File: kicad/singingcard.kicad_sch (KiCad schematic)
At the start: 16 parts, among them J2 Audio_In, SW1 Button, U1 ISD3900FYI, U2 W25Q16JVSSIQ

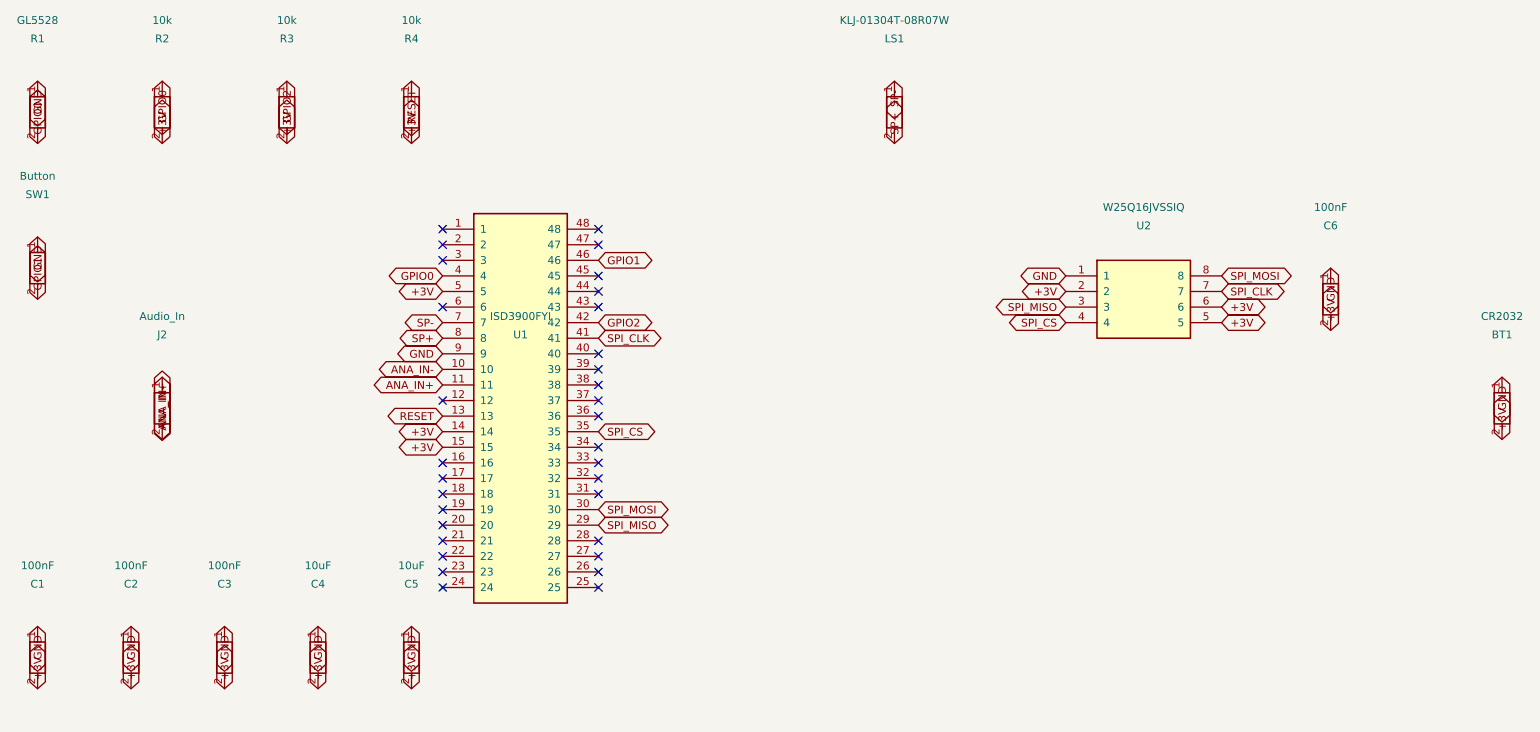
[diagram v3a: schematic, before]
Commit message: Fix global label orientation and U2 3D model offset
Schematic label fixes:
- Fixed label position formula: now uses x + offset*cos(angle) and
  y - offset*sin(angle) to properly offset labels away from components
- Fixed label angle: now uses (angle + 180) % 360 so arrow points
  toward the pin, not away from it
- This resolves labels on left side of chips overlapping with pins
- ERC reduced from 15 to 12 warnings (removed net conflict warnings)

Footprint fixes:
- Fixed U2 (W25Q16JVSSIQ) 3D model offset from (1.65, -2.84, 0) to (0, 0, 0)
- Updated model path to use ${KIPRJMOD} prefix

Skill file updates:
- Updated global label orientation section with correct formulas
- Added "Common mistake" note about Y-axis sign convention
- Added "3D models offset from footprint" troubleshooting section
- Documented easyeda2kicad offset issues and fix

🤖 Generated with [Claude Code](https://claude.com/claude-code)

Co-Authored-By: Claude <noreply@anthropic.com>
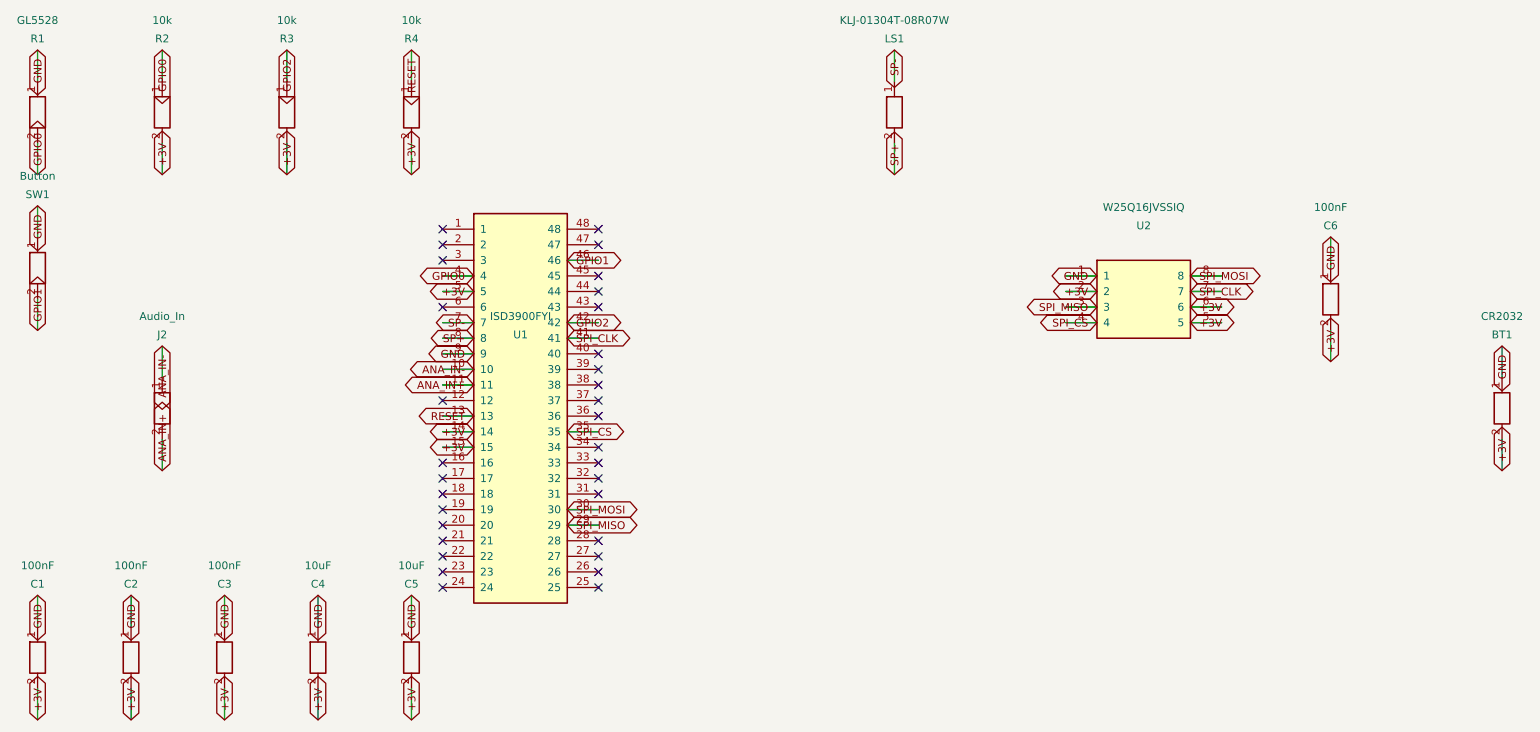
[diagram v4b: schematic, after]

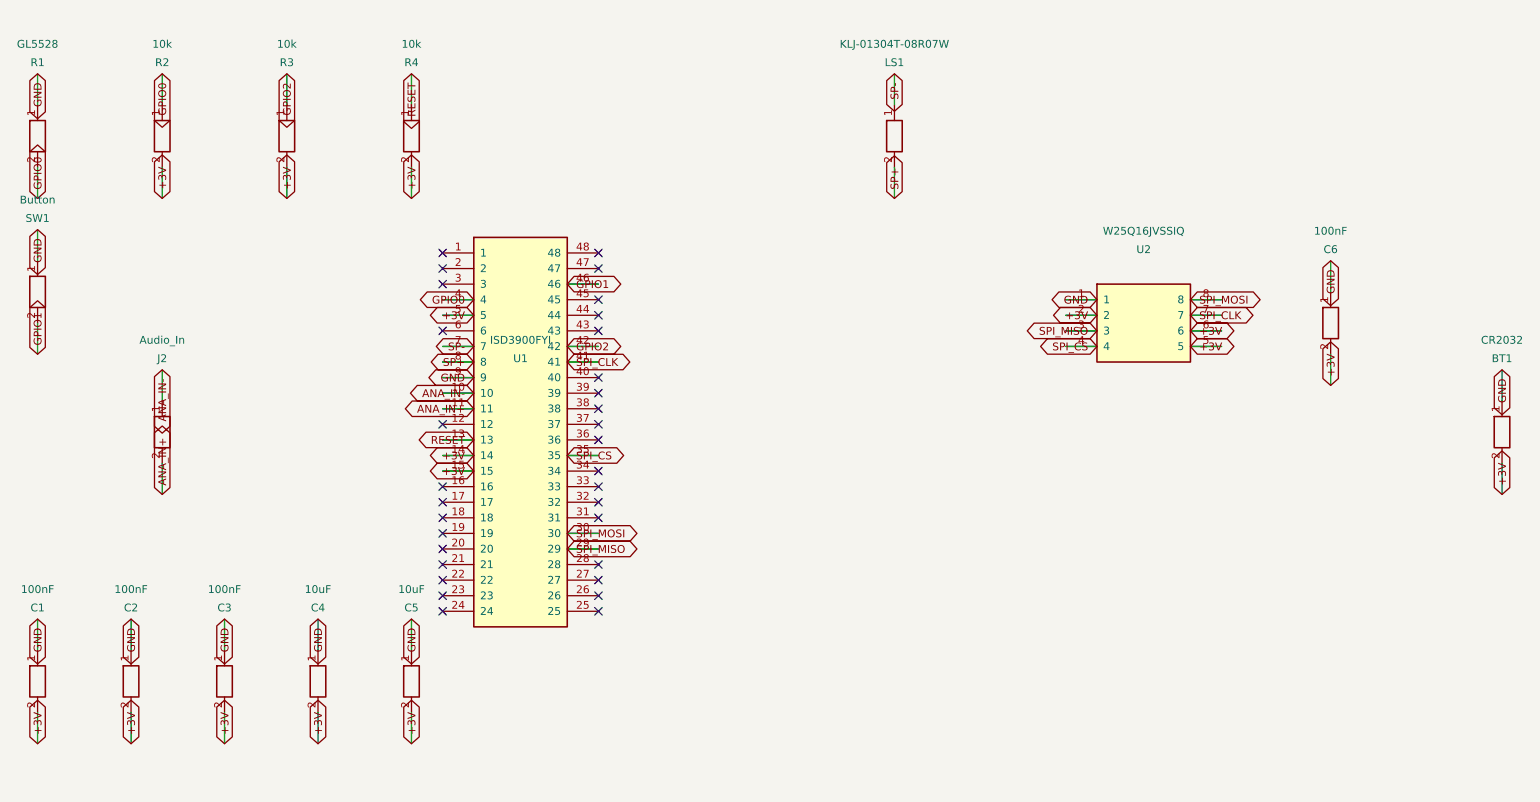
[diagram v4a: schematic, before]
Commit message: Fix global label orientation formula (iteration 2)
Corrected the label placement formula:
- Pin angle points TOWARD component body, not away
- Label offset should be OPPOSITE to pin angle direction
- X formula: x - offset * cos(angle)
- Y formula: y - offset * sin(angle)
- Label angle: same as pin angle (arrow points toward pin)

Labels now correctly placed:
- Left-side IC pins: labels to the LEFT, pointing right
- Right-side IC pins: labels to the RIGHT, pointing left
- Top 2-pin: labels ABOVE, pointing down
- Bottom 2-pin: labels BELOW, pointing up

ERC: 0 errors, 12 warnings (library path warnings only)

🤖 Generated with [Claude Code](https://claude.com/claude-code)

Co-Authored-By: Claude <noreply@anthropic.com>
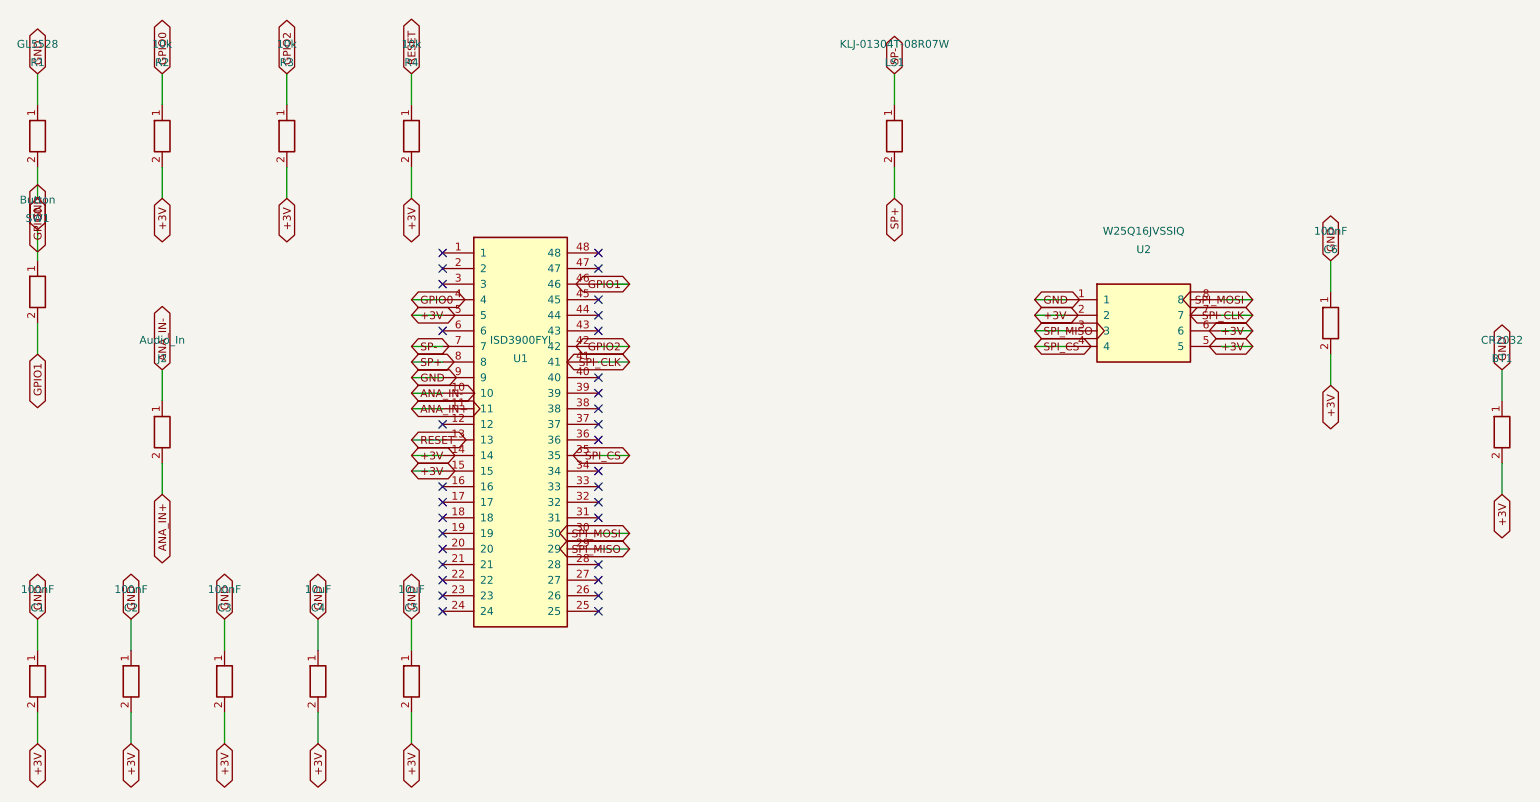
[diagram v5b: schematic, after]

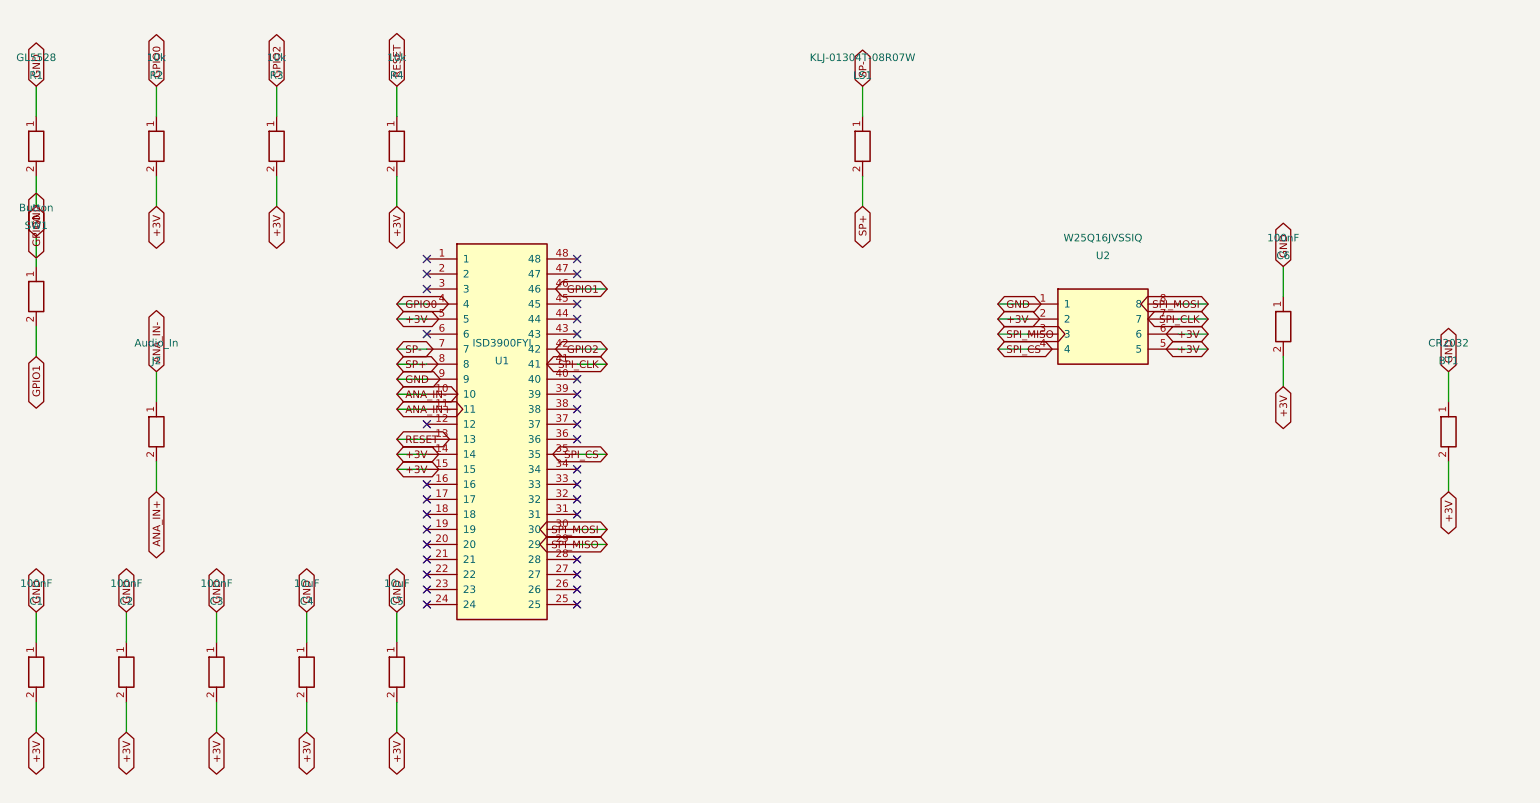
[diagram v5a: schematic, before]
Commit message: Improve schematic readability
Changes:
- Increased label offset from 5.08mm to 7.62mm for better spacing
- Moved reference/value for 2-pin components to the right side
  to avoid overlap with top/bottom pin labels
- Reference designators now clearly visible next to components
- Labels properly separated from component bodies

All 2-pin components (R1-R4, C1-C6, SW1, J2, LS1, BT1) now have:
- Labels above/below for pin connections
- Reference/value text to the right side

ERC: 0 errors, 13 warnings (library path warnings only)

🤖 Generated with [Claude Code](https://claude.com/claude-code)

Co-Authored-By: Claude <noreply@anthropic.com>
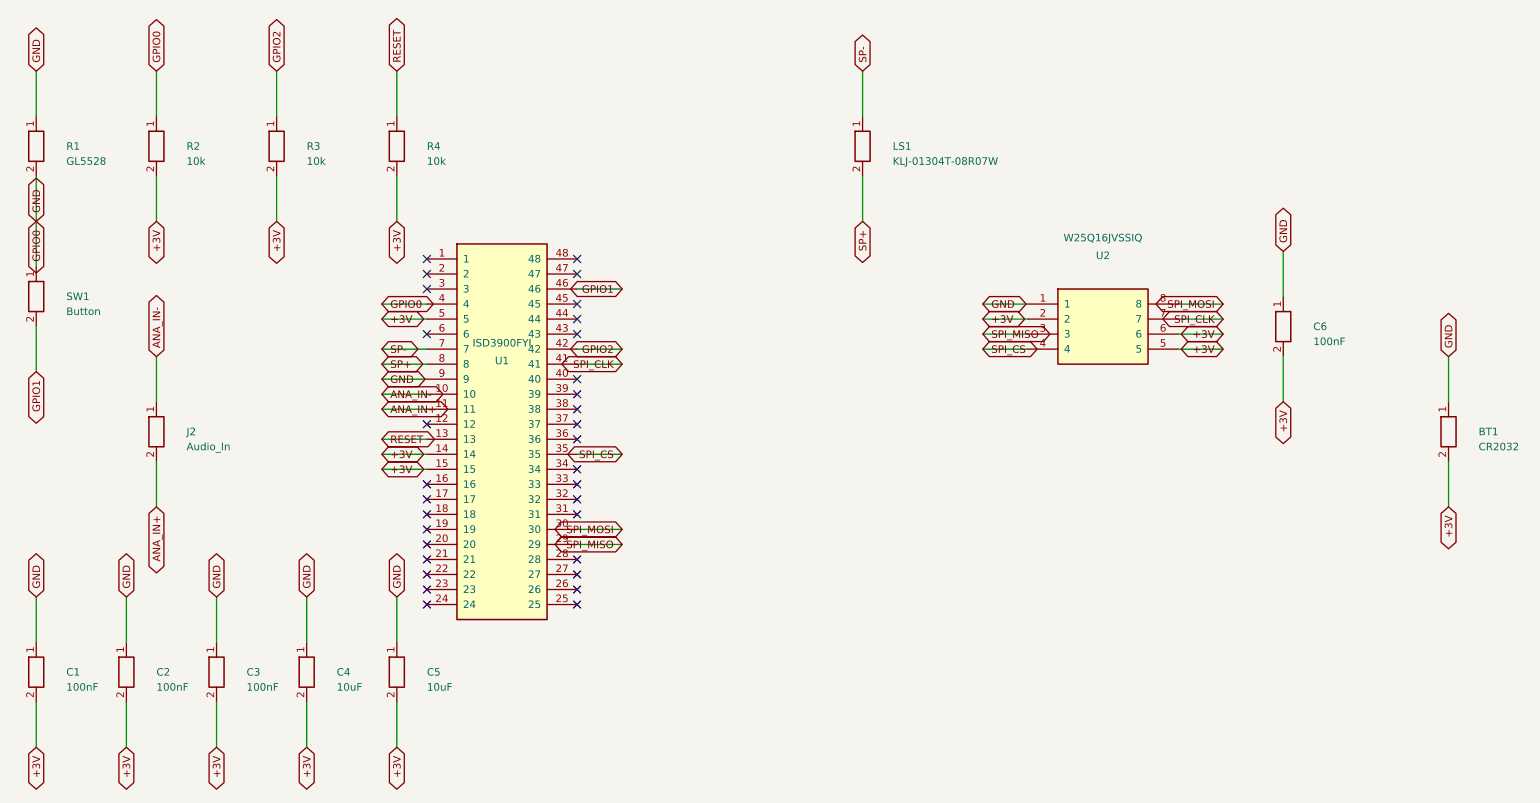
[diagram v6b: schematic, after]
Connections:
- net GPIO0 is gone; now on net GND: R1.2, R2.1, U1.4
